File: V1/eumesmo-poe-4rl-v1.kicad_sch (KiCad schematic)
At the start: 58 parts, among them J1 USB_C_Receptacle_USB2.0, J2 RJ45 JACK, Q1 UMH3N, Q2 WPM2015-3/TR, Q3 LMUN2211LT1G, SW1 RESET, U1 CH340K, U2 ESP32-WROOM-32UE-N16, U3 LAN8710A

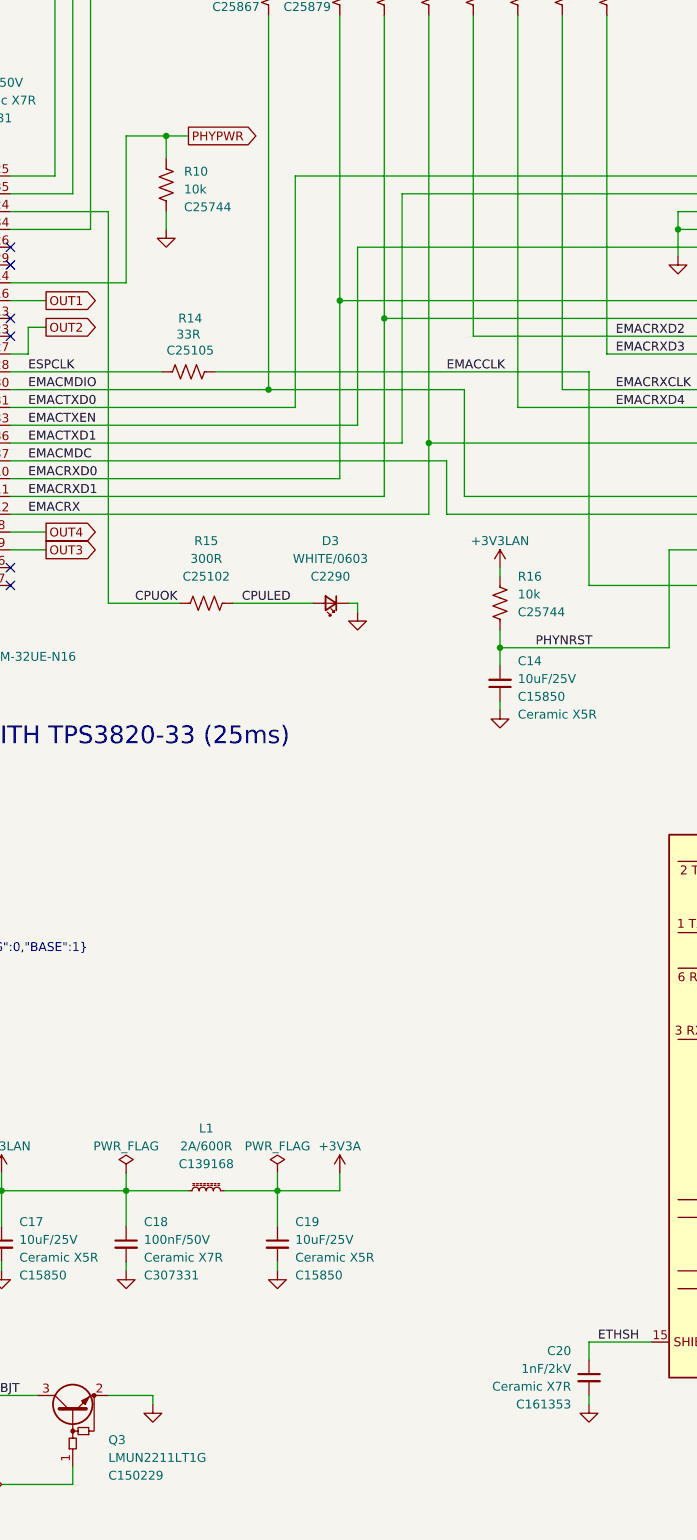
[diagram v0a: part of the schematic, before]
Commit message: Adjusted components according to availability in JLCPCB.
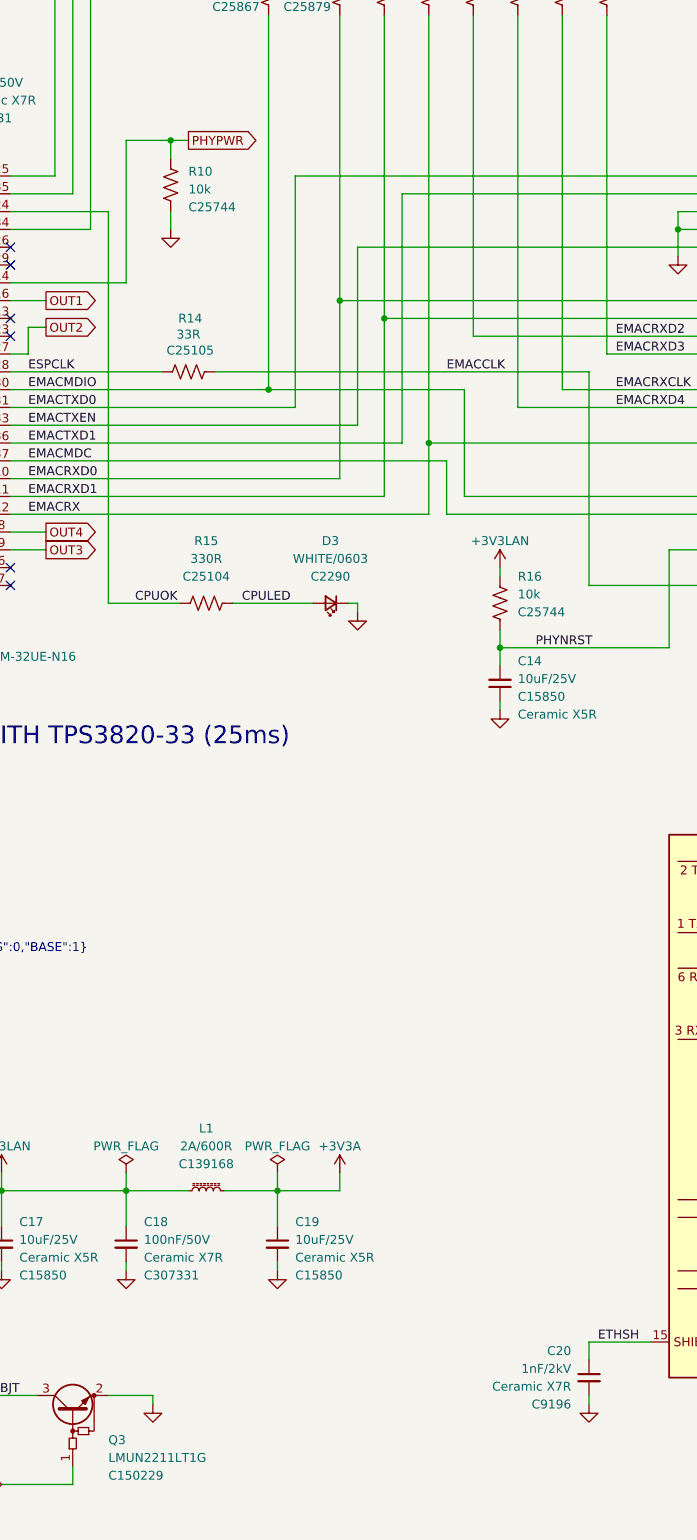
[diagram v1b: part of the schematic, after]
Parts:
- C20: LCSC Part # C161353 -> C9196; Mfr Murata Electronics -> FH; Mfr PN GR431BR7LA102KW66L -> 1206B102K202NT; Vendor PN C161353 -> C9196
- R15: value 300R -> 330R; LCSC Part # C25102 -> C25104; Mfr PN 0402WGF3000TCE -> 0402WGF3300TCE; Package (none) -> 0402/1005; Vendor PN C25102 -> C25104
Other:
- moved on the sheet: R10
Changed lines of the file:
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@@
 	)
 	(junction
-		(at 226.695 59.055)
+		(at 369.57 125.73)
 		(diameter 0)
 		(color 0 0 0 0)
 	)
 	(junction
-		(at 369.57 125.73)
+		(at 227.33 59.69)
 		(diameter 0)
 		(color 0 0 0 0)
@@
 	(wire
 		(pts
+			(xy 220.98 80.01) (xy 220.98 59.69)
+		)
+		(stroke
+			(width 0)
+			(type default)
+		)
+	)
+	(wire
+		(pts
 			(xy 331.47 46.99) (xy 349.25 46.99)
 		)
@@
 	(wire
 		(pts
+			(xy 204.47 80.01) (xy 220.98 80.01)
+		)
+		(stroke
+			(width 0)
+			(type default)
+		)
+	)
+	(wire
+		(pts
 			(xy 203.2 251.46) (xy 213.36 251.46)
 		)
@@
 	(wire
 		(pts
-			(xy 220.98 59.055) (xy 226.695 59.055)
-		)
-		(stroke
-			(width 0)
-			(type default)
-		)
-	)
-	(wire
-		(pts
 			(xy 204.47 110.49) (xy 257.81 110.49)
 		)
@@
 	(wire
 		(pts
-			(xy 226.695 59.055) (xy 229.87 59.055)
+			(xy 21.59 90.17) (xy 21.59 91.44)
 		)
 		(stroke
@@
 	(wire
 		(pts
-			(xy 21.59 90.17) (xy 21.59 91.44)
+			(xy 92.71 68.58) (xy 102.87 68.58)
 		)
 		(stroke
@@
 	(wire
 		(pts
-			(xy 92.71 68.58) (xy 102.87 68.58)
+			(xy 29.21 88.9) (xy 29.21 90.17)
 		)
 		(stroke
@@
 	(wire
 		(pts
-			(xy 29.21 88.9) (xy 29.21 90.17)
+			(xy 270.51 31.75) (xy 264.16 31.75)
 		)
 		(stroke
@@
 	(wire
 		(pts
-			(xy 270.51 31.75) (xy 264.16 31.75)
+			(xy 356.87 33.02) (xy 356.87 29.21)
 		)
 		(stroke
@@
 	(wire
 		(pts
-			(xy 356.87 33.02) (xy 356.87 29.21)
+			(xy 388.62 121.92) (xy 388.62 125.73)
 		)
 		(stroke
@@
 	(wire
 		(pts
-			(xy 388.62 121.92) (xy 388.62 125.73)
+			(xy 227.33 69.85) (xy 227.33 72.39)
 		)
 		(stroke
@@
 	(wire
 		(pts
-			(xy 220.98 80.01) (xy 220.98 59.055)
+			(xy 129.54 76.2) (xy 129.54 81.28)
 		)
 		(stroke
@@
 	(wire
 		(pts
-			(xy 129.54 76.2) (xy 129.54 81.28)
+			(xy 264.16 102.87) (xy 303.53 102.87)
 		)
 		(stroke
@@
 	(wire
 		(pts
-			(xy 264.16 102.87) (xy 303.53 102.87)
+			(xy 46.99 43.18) (xy 46.99 45.72)
 		)
 		(stroke
@@
 	(wire
 		(pts
-			(xy 46.99 43.18) (xy 46.99 45.72)
+			(xy 193.04 224.79) (xy 193.04 227.33)
 		)
 		(stroke
@@
 	(wire
 		(pts
-			(xy 193.04 224.79) (xy 193.04 227.33)
+			(xy 220.98 59.69) (xy 227.33 59.69)
 		)
 		(stroke
@@
 	(wire
 		(pts
-			(xy 204.47 80.01) (xy 220.98 80.01)
-		)
-		(stroke
-			(width 0)
-			(type default)
-		)
-	)
-	(wire
-		(pts
 			(xy 46.99 68.58) (xy 46.99 71.12)
 		)
@@
 	(wire
 		(pts
-			(xy 226.695 69.85) (xy 226.695 72.39)
-		)
-		(stroke
-			(width 0)
-			(type default)
-		)
-	)
-	(wire
-		(pts
 			(xy 210.82 21.59) (xy 210.82 22.86)
 		)
@@
 	(wire
 		(pts
-			(xy 226.695 59.055) (xy 226.695 62.23)
+			(xy 336.55 195.58) (xy 336.55 200.66)
 		)
 		(stroke
@@
 	(wire
 		(pts
-			(xy 336.55 195.58) (xy 336.55 200.66)
+			(xy 383.54 132.08) (xy 388.62 132.08)
 		)
 		(stroke
@@
 	(wire
 		(pts
-			(xy 383.54 132.08) (xy 388.62 132.08)
+			(xy 87.63 38.1) (xy 91.44 38.1)
 		)
 		(stroke
@@
 	(wire
 		(pts
-			(xy 87.63 38.1) (xy 91.44 38.1)
+			(xy 158.75 207.01) (xy 158.75 209.55)
 		)
 		(stroke
@@
 	(wire
 		(pts
-			(xy 158.75 207.01) (xy 158.75 209.55)
+			(xy 227.33 59.69) (xy 229.87 59.69)
 		)
 		(stroke
@@
 	(wire
 		(pts
+			(xy 227.33 59.69) (xy 227.33 62.23)
+		)
+		(stroke
+			(width 0)
+			(type default)
+		)
+	)
+	(wire
+		(pts
 			(xy 204.47 118.11) (xy 209.55 118.11)
 		)
@@
 	(global_label "PHYPWR"
 		(shape output)
-		(at 229.87 59.055 0)
+		(at 229.87 59.69 0)
 		(fields_autoplaced yes)
 		(effects
@@
 		)
 		(property "Intersheetrefs" "${INTERSHEET_REFS}"
-			(at 239.8815 59.055 0)
+			(at 239.8815 59.69 0)
 			(hide yes)
 			(show_name no)
@@
 			)
 		)
-		(property "Value" "300R"
+		(property "Value" "330R"
 			(at 232.41 119.38 90)
 			(show_name no)
@@
 			)
 		)
-		(property "Mfr PN" "0402WGF3000TCE"
+		(property "Mfr PN" "0402WGF3300TCE"
 			(at 232.41 125.73 0)
 			(hide yes)
@@
 			)
 		)
-		(property "Vendor PN" "C25102"
+		(property "Vendor PN" "C25104"
 			(at 232.41 125.73 0)
 			(hide yes)
@@
 			)
 		)
-		(property "LCSC Part #" "C25102"
+		(property "LCSC Part #" "C25104"
 			(at 232.41 121.92 90)
 			(show_name no)
@@
 			)
 		)
+		(property "Package" "0402/1005"
+			(at 232.41 125.73 90)
+			(hide yes)
+			(show_name no)
+			(do_not_autoplace no)
+			(effects
+				(font
+					(size 1.27 1.27)
+				)
+			)
+		)
 		(pin "1"
 		)
@@
 			)
 		)
-		(property "LCSC Part #" "C161353"
+		(property "LCSC Part #" "C9196"
 			(at 284.48 240.03 0)
 			(show_name no)
@@
 			)
 		)
-		(property "Mfr" "Murata Electronics"
+		(property "Mfr" "FH"
 			(at 287.02 236.22 0)
 			(hide yes)
@@
 			)
 		)
-		(property "Mfr PN" "GR431BR7LA102KW66L"
+		(property "Mfr PN" "1206B102K202NT"
 			(at 287.02 236.22 0)
 			(hide yes)
@@
 			)
 		)
-		(property "Vendor PN" "C161353"
+		(property "Vendor PN" "C9196"
 			(at 287.02 236.22 0)
 			(hide yes)
@@
 	(symbol
 		(lib_id "Device:R_US")
-		(at 226.695 66.04 180)
+		(at 227.33 66.04 180)
 		(unit 1)
 		(body_style 1)
@@
 		(fields_autoplaced yes)
 		(property "Reference" "R10"
-			(at 229.235 64.135 0)
+			(at 229.87 64.135 0)
 			(show_name no)
 			(do_not_autoplace no)
@@
 		)
 		(property "Value" "10k"
-			(at 229.235 66.675 0)
+			(at 229.87 66.675 0)
 			(show_name no)
 			(do_not_autoplace no)
@@
 		)
 		(property "Footprint" "Tales:R_0402_1005Metric"
-			(at 225.679 65.786 90)
+			(at 226.314 65.786 90)
 			(hide yes)
 			(show_name no)
@@
 		)
 		(property "Datasheet" ""
-			(at 226.695 66.04 0)
+			(at 227.33 66.04 0)
 			(hide yes)
 			(show_name no)
@@
 		)
 		(property "Description" "Resistor, US symbol"
-			(at 226.695 66.04 0)
+			(at 227.33 66.04 0)
 			(hide yes)
 			(show_name no)
@@
 		)
 		(property "Mfr" "Uniroyal"
-			(at 226.695 66.04 0)
+			(at 227.33 66.04 0)
 			(hide yes)
 			(show_name no)
@@
 		)
 		(property "Vendor" "JLCPCB"
-			(at 226.695 66.04 0)
+			(at 227.33 66.04 0)
 			(hide yes)
 			(show_name no)
@@
 		)
 		(property "Mfr PN" "0402WGF1002TCE"
-			(at 226.695 66.04 0)
+			(at 227.33 66.04 0)
 			(hide yes)
 			(show_name no)
@@
 		)
 		(property "Technology" "1%"
-			(at 226.695 66.04 0)
+			(at 227.33 66.04 0)
 			(hide yes)
 			(show_name no)
@@
 		)
 		(property "Vendor PN" "C25744"
-			(at 226.695 66.04 0)
+			(at 227.33 66.04 0)
 			(hide yes)
 			(show_name no)
@@
 		)
 		(property "LCSC Part #" "C25744"
-			(at 229.235 69.215 0)
+			(at 229.87 69.215 0)
 			(show_name no)
 			(do_not_autoplace no)
@@
 		)
 		(property "JLCPCB BOM" "1"
-			(at 226.695 66.04 0)
+			(at 227.33 66.04 0)
 			(hide yes)
 			(show_name no)
@@
 		)
 		(property "Package" "0402/1005"
-			(at 226.695 66.04 0)
+			(at 227.33 66.04 0)
 			(hide yes)
 			(show_name no)
@@
 	(symbol
 		(lib_id "power:GND")
-		(at 226.695 72.39 0)
+		(at 227.33 72.39 0)
 		(unit 1)
 		(body_style 1)
@@
 		(fields_autoplaced yes)
 		(property "Reference" "#PWR021"
-			(at 226.695 78.74 0)
+			(at 227.33 78.74 0)
 			(hide yes)
 			(show_name no)
@@
 		)
 		(property "Value" "GND"
-			(at 226.695 77.47 0)
+			(at 227.33 77.47 0)
 			(hide yes)
 			(show_name no)
@@
 		)
 		(property "Footprint" ""
-			(at 226.695 72.39 0)
+			(at 227.33 72.39 0)
 			(hide yes)
 			(show_name no)
@@
 		)
 		(property "Datasheet" ""
-			(at 226.695 72.39 0)
+			(at 227.33 72.39 0)
 			(hide yes)
 			(show_name no)
@@
 		)
 		(property "Description" "Power symbol creates a global label with name \"GND\" , ground"
-			(at 226.695 72.39 0)
+			(at 227.33 72.39 0)
 			(hide yes)
 			(show_name no)
